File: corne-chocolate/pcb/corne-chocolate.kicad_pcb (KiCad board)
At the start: 2 copper layers, 236.4 x 91.4 mm, 150 parts, among them J1 Conn_01x04, J2 54-00174, J3 781271220, J4 54-00174, P1 Conn_01x01, P2 Conn_01x01, SW1 SW_PUSH, SW10 SW_PUSH, SW11 SW_PUSH, SW12 SW_PUSH, SW13 SW_PUSH, SW14 SW_PUSH, SW15 SW_PUSH, SW16 SW_PUSH, SW17 SW_PUSH, SW18 SW_PUSH, SW19 SW_PUSH, SW2 SW_PUSH, SW20 SW_PUSH, SW21 SW_PUSH, SW22 SW_PUSH, SW23 SW_PUSH, SW24 SW_PUSH, SW25 SW_PUSH, SW26 SW_PUSH, SW27 SW_PUSH, SW28 SW_PUSH, SW29 SW_PUSH, SW3 SW_PUSH, SW30 SW_PUSH, SW31 SW_PUSH, SW32 SW_PUSH, SW33 SW_PUSH, SW34 SW_PUSH, SW35 SW_PUSH, SW36 SW_PUSH, SW4 SW_PUSH, SW5 SW_PUSH, SW6 SW_PUSH, SW7 SW_PUSH, SW8 SW_PUSH, SW9 SW_PUSH, U1 ProMicro, U2 ProMicro

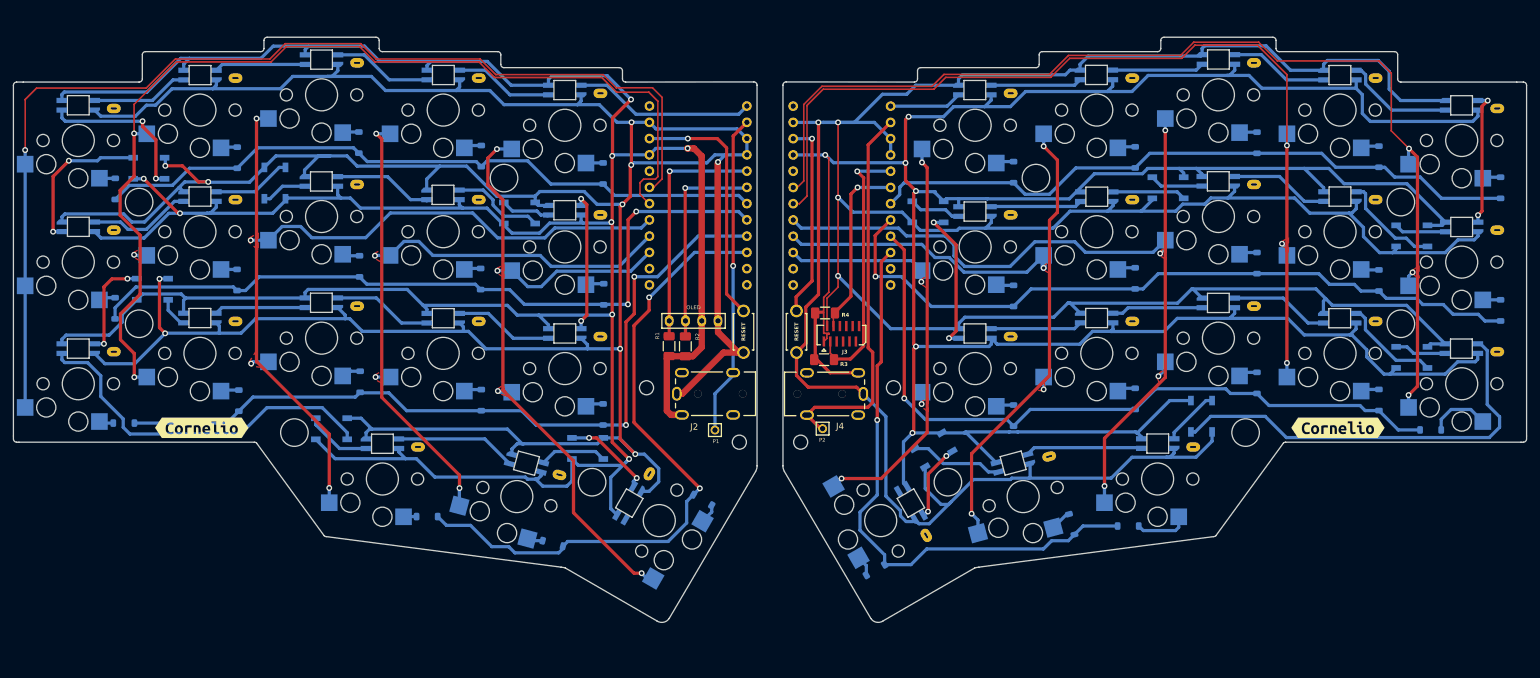
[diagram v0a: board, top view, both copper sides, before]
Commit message: breakaway tabs
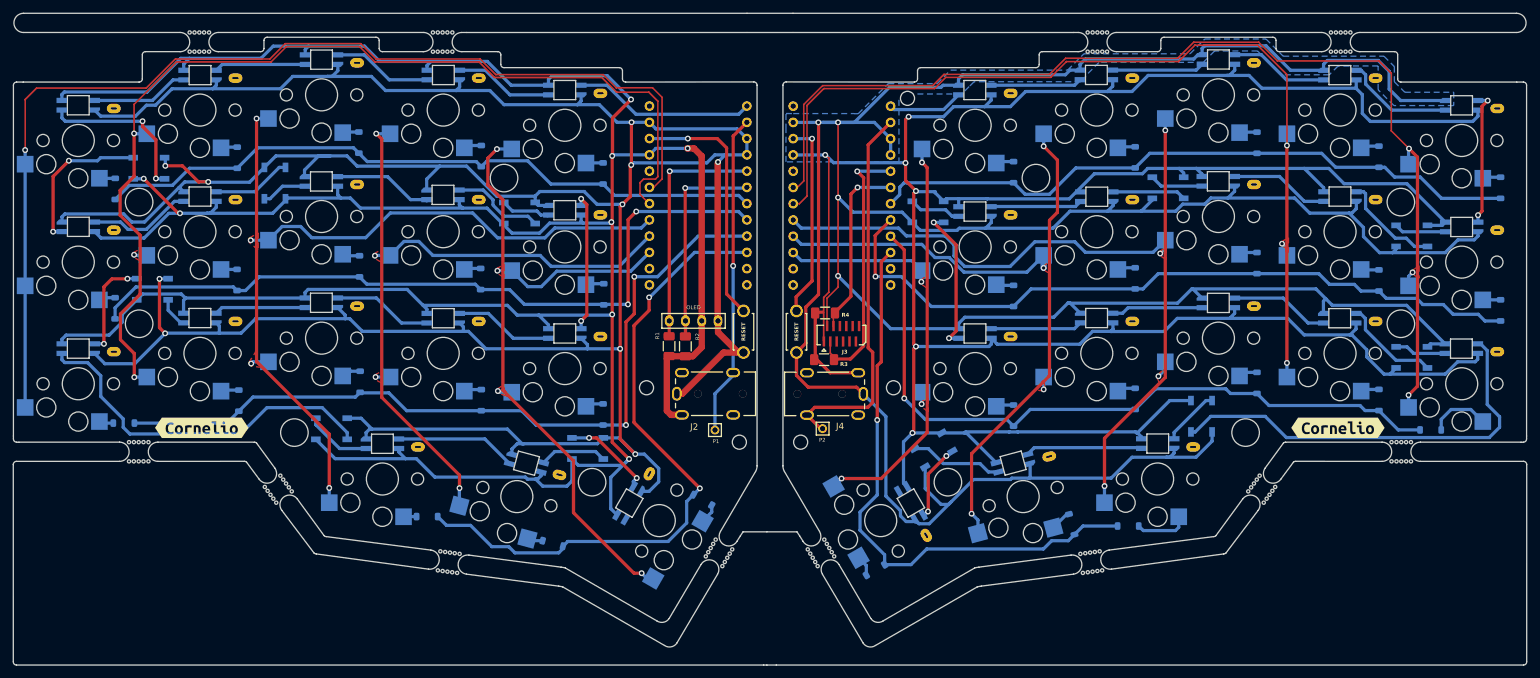
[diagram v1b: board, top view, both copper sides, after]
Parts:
- added H15: MountingHole, MountingHole:MountingHole_2.2mm_M2_ISO14580, F.Cu at (169.2, 66.6)
- added mouse-bite-3mm-slot: VAL**, kbd:mouse-bite-3mm-slot, F.Cu at (70.9, 127.7)
- added mouse-bite-3mm-slot: VAL**, kbd:mouse-bite-3mm-slot, B.Cu at (236.8, 57.9)
- added mouse-bite-3mm-slot: VAL**, kbd:mouse-bite-3mm-slot, B.Cu at (246.3, 121.8)
- added mouse-bite-3mm-slot: VAL**, kbd:mouse-bite-3mm-slot, B.Cu at (155.7, 137.6)
- added mouse-bite-3mm-slot: VAL**, kbd:mouse-bite-3mm-slot, F.Cu at (58.5, 57.9)
- added mouse-bite-3mm-slot: VAL**, kbd:mouse-bite-3mm-slot, F.Cu at (97.5, 139.1)
- added mouse-bite-3mm-slot: VAL**, kbd:mouse-bite-3mm-slot, F.Cu at (96.5, 57.9)
- added mouse-bite-3mm-slot: VAL**, kbd:mouse-bite-3mm-slot, F.Cu at (49.1, 121.8)
- added mouse-bite-3mm-slot: VAL**, kbd:mouse-bite-3mm-slot, F.Cu at (139.7, 137.7)
- added mouse-bite-3mm-slot: VAL**, kbd:mouse-bite-3mm-slot, B.Cu at (197.9, 139.1)
- added mouse-bite-3mm-slot: VAL**, kbd:mouse-bite-3mm-slot, B.Cu at (224.5, 127.7)
- added mouse-bite-3mm-slot: VAL**, kbd:mouse-bite-3mm-slot, B.Cu at (198.8, 57.9)
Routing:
- net RVCC: track 490.9 -> 489.6 mm
- added copper zone on B.Cu, net RGND
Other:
- board size 236.4 x 91.4 mm -> 236.4 x 101.8 mm

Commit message: zones in right keyboard
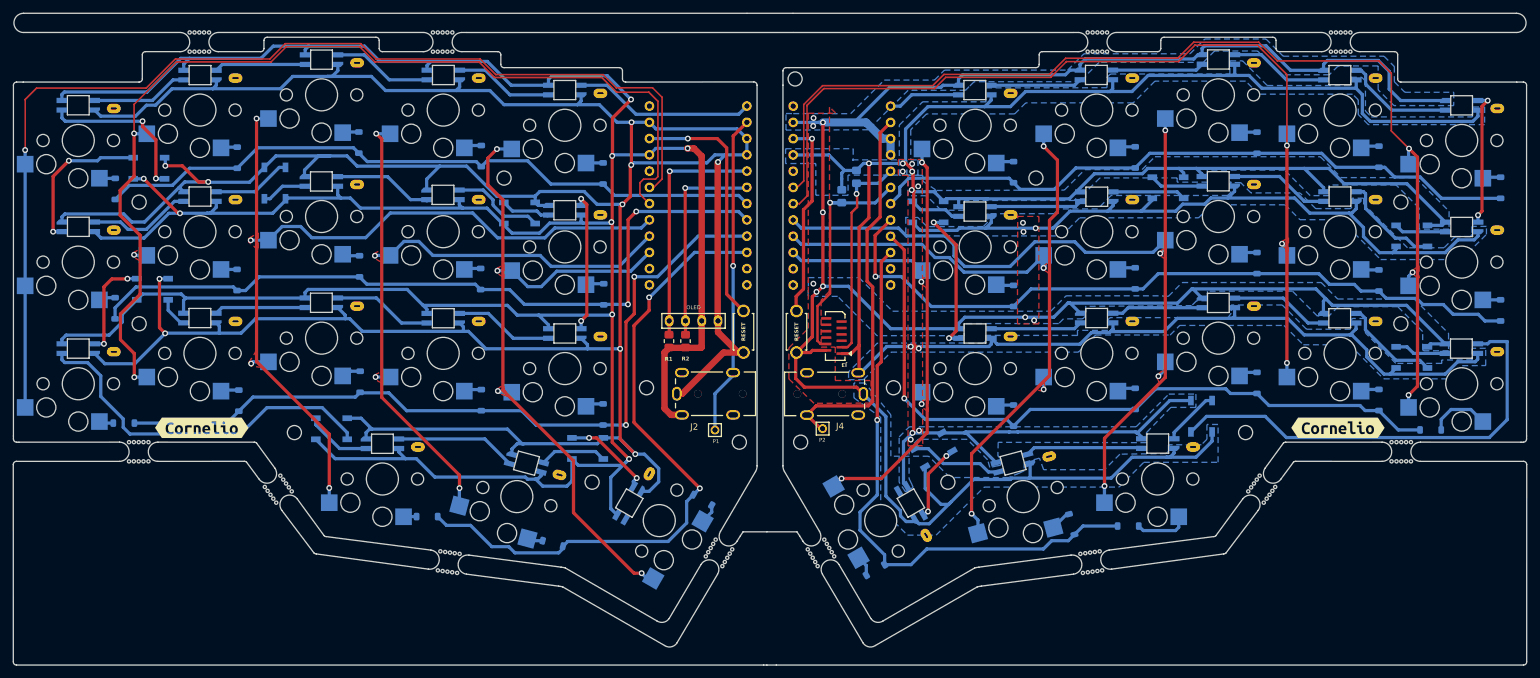
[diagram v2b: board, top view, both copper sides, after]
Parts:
- H10, H11, H12, H13, H14, H3, H4, H5, H6, H7: footprint MountingHole:MountingHole_4.3mm_M4_ISO14580 -> MountingHole:MountingHole_2.2mm_M2_ISO14580
- R1, R2: footprint Resistor_SMD:R_1206_3216Metric_Pad1.30x1.75mm_HandSolder -> kbd:R_0805_2012Metric_Pad1.20x1.40mm_HandSolder
- R3, R4: footprint kbd:R_1206_3216Metric_Pad1.30x1.75mm_HandSolder -> kbd:R_0805_2012Metric_Pad1.20x1.40mm_HandSolder; moved to B.Cu
- moved R3 29.0 mm to (161.2, 78.9), turned to -90 degrees
- moved R4 18.4 mm to (158.9, 81.9), turned to -90 degrees
- moved H15 17.8 mm to (151.6, 63.6)
- moved J3 1.23 mm to (157.7, 103.8), turned to 90 degrees
- moved R2 0.81 mm to (134.5, 104.6)
- moved R1 0.79 mm to (131.9, 104.6)
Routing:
- net RGND: track 543.5 -> 505.2 mm, vias 4 -> 12
- net RSCL: track 28.4 -> 36.3 mm
- net RSDA: track 41.2 -> 33.3 mm
- net RVCC: track 489.6 -> 495.3 mm, vias 6 -> 12
- net Net-(LED43-DOUT): track 66.0 -> 69.9 mm
- net LVCC: track 498.6 -> 499.7 mm
- added copper zone on F.Cu, net RGND
- added copper zone on B.Cu, net RVCC
- added copper zone on F.Cu, net RVCC
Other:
- outline, holes or cut-outs redrawn

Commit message: zones in left keyboard
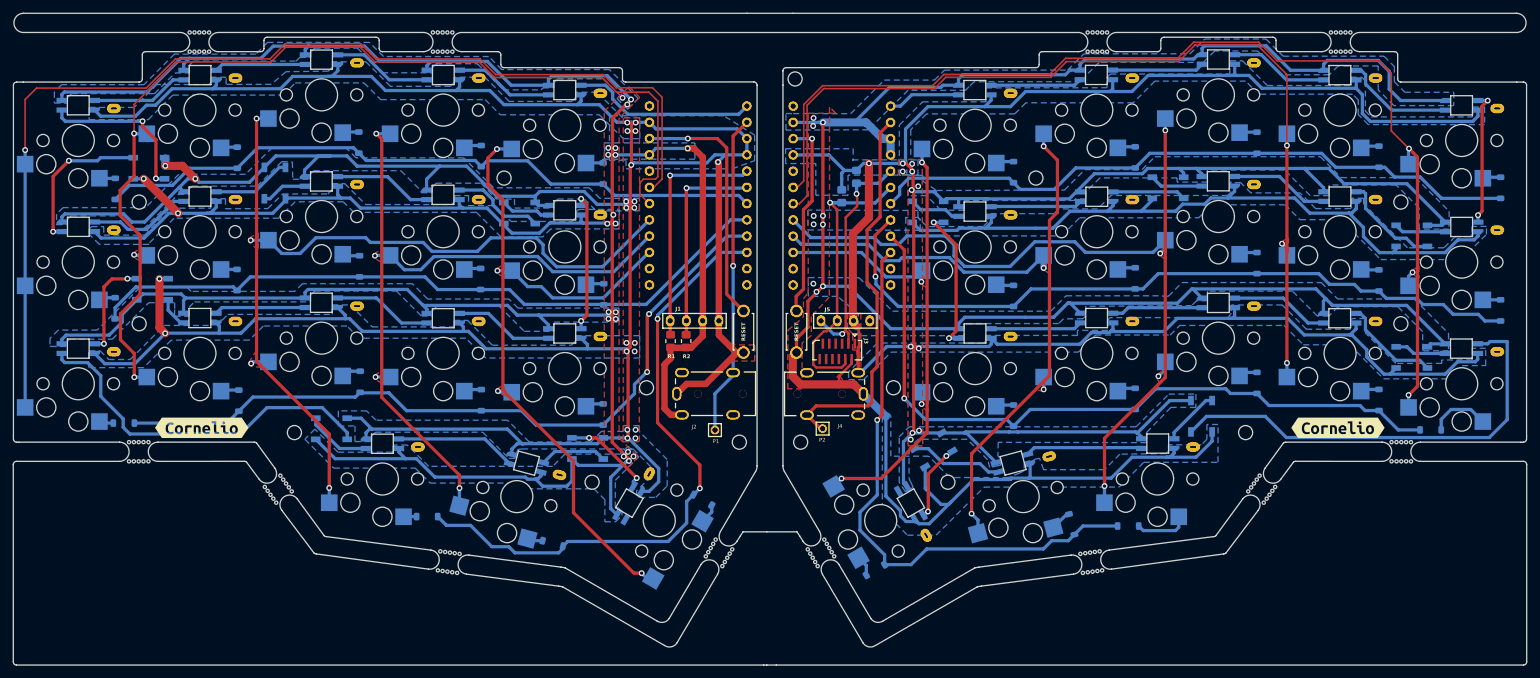
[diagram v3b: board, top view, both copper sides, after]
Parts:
- added J5: Conn_01x04, kbd:OLED_1side, F.Cu at (155.7, 101.4)
- moved J3 2.46 mm to (158.2, 106.2), turned to 180 degrees
- moved R1 0.25 mm to (132.2, 104.6)
- moved J1 0.15 mm to (132.1, 101.4)
- moved R2 0.10 mm to (134.6, 104.6)
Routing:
- net RSCL: track 36.3 -> 46.0 mm
- net Lrow1: track 118.9 -> 110.1 mm, vias 2 -> 0
- net Lrow2: track 124.8 -> 118.0 mm
- net Lrow3: track 102.9 -> 97.4 mm
- net RSDA: track 33.3 -> 37.1 mm, vias 1 -> 2
- net Lcol3: track 137.7 -> 141.1 mm
- net LGND: track 528.4 -> 525.2 mm, vias 10 -> 22
- net RVCC: track 495.3 -> 492.8 mm
- net Lcol5: track 111.5 -> 112.9 mm
- net Rcol3: track 134.5 -> 135.6 mm
- net RGND: track 505.2 -> 506.2 mm, vias 12 -> 10
- net LSDA: track 38.1 -> 37.2 mm
- net LVCC: track 499.7 -> 498.8 mm, vias 8 -> 21
- net Rcol5: track 87.7 -> 88.5 mm
- net Rrow1: track 114.6 -> 115.4 mm
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- added copper zone on B.Cu, net LGND
- added copper zone on F.Cu, net LGND
- added copper zone on B.Cu, net LVCC
- added copper zone on F.Cu, net LVCC
